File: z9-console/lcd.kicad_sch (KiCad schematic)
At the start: 17 parts, among them J10 Conn_01x04_Pin, J2 LCD 3.2" 240x320 Conn_01x14_P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, J8 Conn_01x14_Pin, J9 Conn_01x18_Pin, Q2 AO3400A, Q4 NPN, U7 SN74LVC1G14DRLR, U8 XC6206PxxxMR

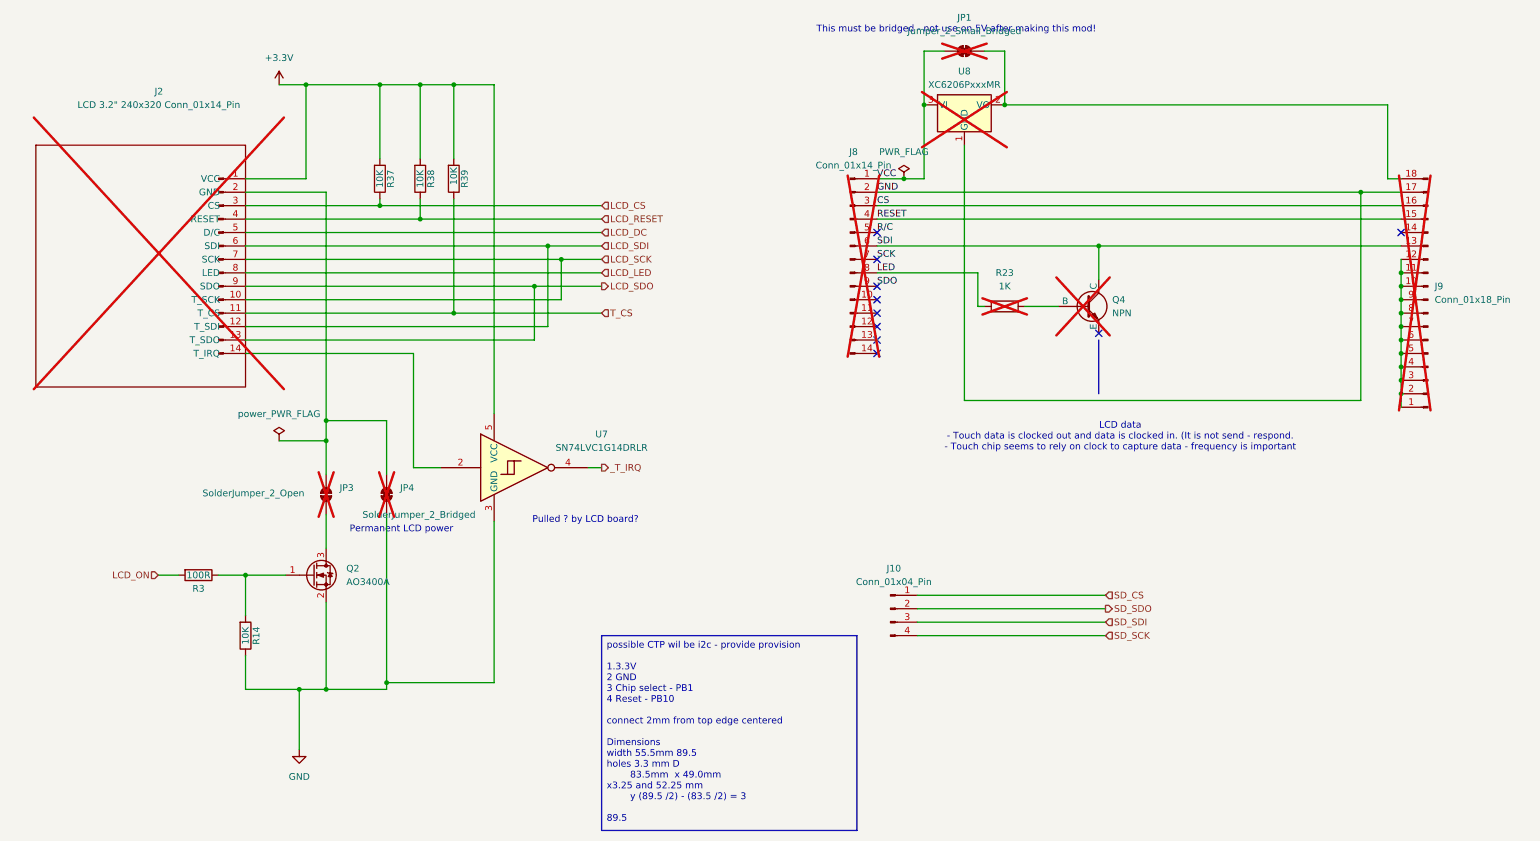
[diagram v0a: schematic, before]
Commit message: lcd power switch-- add new accelerometer
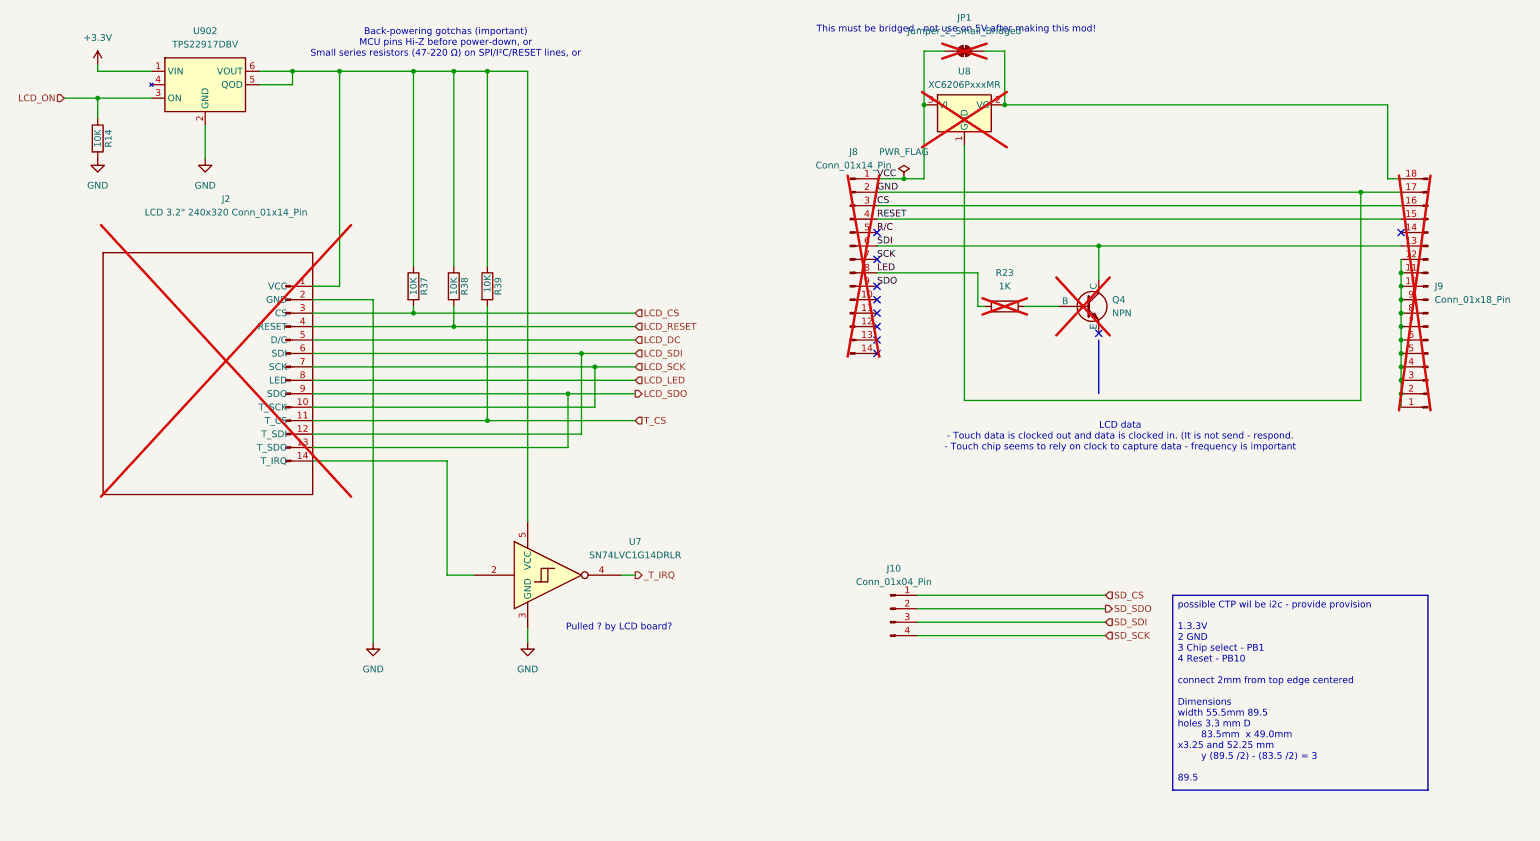
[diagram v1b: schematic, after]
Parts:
- removed JP3: SolderJumper_2_Open, Jumper:SolderJumper-2_P1.3mm_Open_TrianglePad1.0x1.5mm, symbol Jumper:SolderJumper_2_Open
- removed JP4: SolderJumper_2_Bridged, Jumper:SolderJumper-2_P1.3mm_Bridged_Pad1.0x1.5mm, symbol Jumper:SolderJumper_2_Bridged
- removed Q2: AO3400A, Package_TO_SOT_SMD:SOT-23, symbol dnt_global:AO3400A
- removed R3: 100R, Resistor_SMD:R_0603_1608Metric, symbol Device:R
- added U902: TPS22917DBV, dnt:SOT-363_SC-70-6, symbol dnt_global:TPS22919DCKR
- R14, R37, R38, R39: footprint Resistor_SMD:R_0603_1608Metric -> PCM_JLCPCB:R_0402; symbol Device:R -> dnt_global:Resistor_0402,10kΩ; Attrition Qty (none) -> 10; Category (none) -> Resistors,Chip Resistor - Surface Mount; Class (none) -> Basic Component; LCSC C25804 -> C25744; Manufacturer (none) -> UNI-ROYAL(Uniroyal Elec); Minimum Qty (none) -> 20; Operating Temperature Range (none) -> -55°C~+155°C; Overload Voltage (Max) (none) -> 50V; Part (none) -> 0402WGF1002TCE; Power(Watts) (none) -> 62.5mW; Price (none) -> 0.004USD; Process (none) -> SMT; Resistance (none) -> 10kΩ; Stock (none) -> 24372091; Temperature Coefficient (none) -> ±100ppm/°C; Tolerance (none) -> ±1%; Type (none) -> Thick Film Resistors
- R23: footprint Resistor_SMD:R_0201_0603Metric -> PCM_JLCPCB:R_0402; symbol Device:R -> dnt_global:Resistor_0402,10kΩ; Attrition Qty (none) -> 10; Category (none) -> Resistors,Chip Resistor - Surface Mount; Class (none) -> Basic Component; LCSC (none) -> C25744; Manufacturer (none) -> UNI-ROYAL(Uniroyal Elec); Minimum Qty (none) -> 20; Operating Temperature Range (none) -> -55°C~+155°C; Overload Voltage (Max) (none) -> 50V; Part (none) -> 0402WGF1002TCE; Power(Watts) (none) -> 62.5mW; Price (none) -> 0.004USD; Process (none) -> SMT; Resistance (none) -> 10kΩ; Stock (none) -> 24372091; Temperature Coefficient (none) -> ±100ppm/°C; Tolerance (none) -> ±1%; Type (none) -> Thick Film Resistors
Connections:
- net +3.3V: now also U902.1 (VIN); no longer J2.1 (VCC), R37.2, R38.2, R39.2, U7.5 (VCC)
- net GND: now also J2.2 (GND), U902.2 (GND)
- net LCD_ON: now also R14.2, U902.3 (ON)
- new net: J2.1 (VCC), R37.2, R38.2, R39.2, U7.5 (VCC), U902.5 (QOD), U902.6 (VOUT)
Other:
- note added: "Back-powering gotchas (important) MCU pins Hi-Z before power-down, or Small series resistors (47-220 Ω) on SPI/I²C/RESET lines, or"
- note removed: "Permanent LCD power"
- moved on the sheet: J2, R14, R37, R38, R39, U7

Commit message: change MEMS device
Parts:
- renumbered J8 to J3, J10 to J4, J9 to J5, JP1 to JP2, Q4 to Q2, R14 to R2, R37 to R3, R38 to R4, R39 to R5, R23 to R6, U902 to U2, U7 to U3, U8 to U4
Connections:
- net +3.3V: now also U3.5 (VCC)
- net at J2.1 (VCC), R3.2, R4.2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: no longer U3.5 (VCC)
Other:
- note added: "Pulled low by LCD board on touch - needs invertor"
- note removed: "Pulled ? by LCD board?"
- moved on the sheet: J4

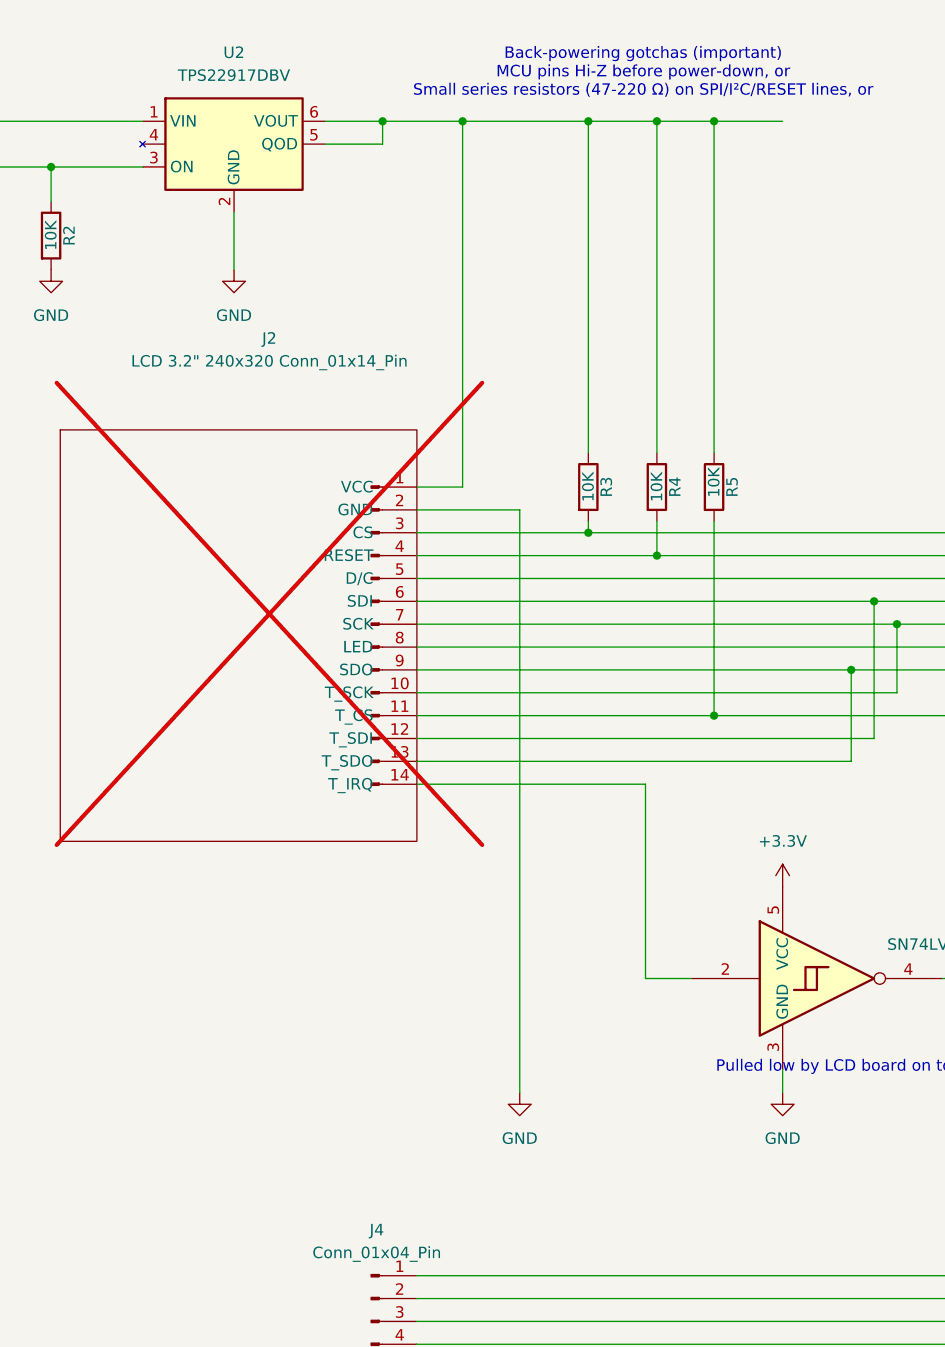
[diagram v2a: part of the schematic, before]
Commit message: drc con - fix ti switch reference  - fix stm32  bypass
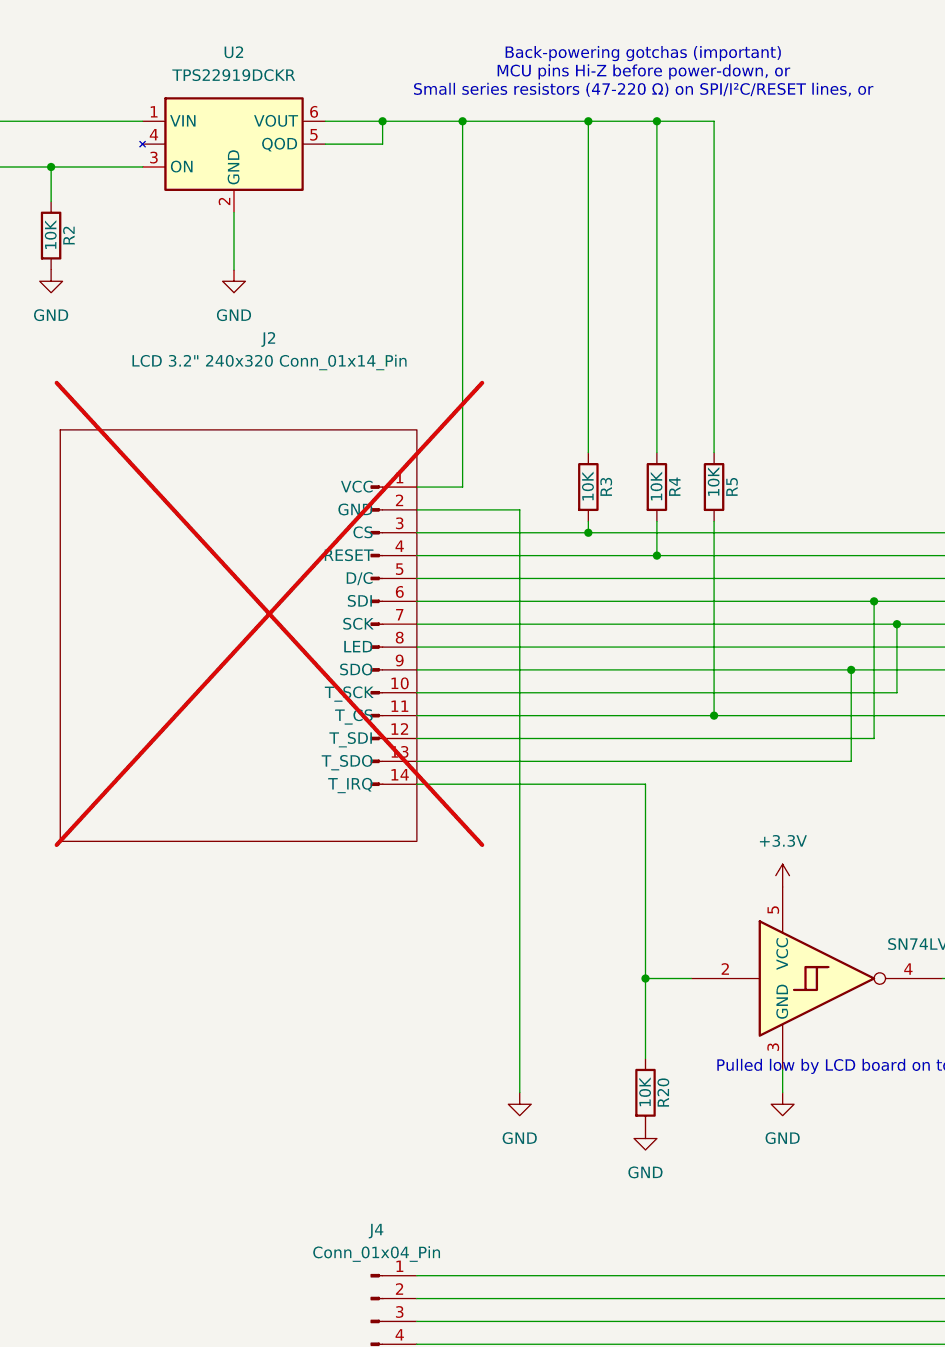
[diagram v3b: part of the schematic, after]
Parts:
- added R20: 10K, PCM_JLCPCB:R_0402, symbol dnt_global:Resistor_0402,10kΩ
- U2: value TPS22917DBV -> TPS22919DCKR
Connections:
- net GND: now also R20.1
- net at J2.14 (T_IRQ), U3.2: now also R20.2

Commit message: lcsc components and cleanup
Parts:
- U2: LCSC (none) -> C2149796
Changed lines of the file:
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@@
+			)
+		)
+		(property "LCSC" "C2149796"
+			(at 51.308 15.748 0)
+			(effects
+				(font
+					(size 1.27 1.27)
+				)
+				(hide yes)
 			)
 		)

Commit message: lcsc changes done - export for prod
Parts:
- R2, R20, R3, R4, R5: footprint PCM_JLCPCB:R_0402 -> dnt:R_0402_1005Metric; symbol dnt_global:Resistor_0402,10kΩ -> dnt_global:0402,10kΩ
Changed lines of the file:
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@@
 	)
 	(symbol
-		(lib_id "dnt_global:Resistor_0402,10kΩ")
+		(lib_id "dnt_global:0402,10kΩ")
 		(at 104.14 63.5 0)
 		(mirror x)
@@
 			)
 		)
-		(property "Footprint" "PCM_JLCPCB:R_0402"
+		(property "Footprint" "dnt:R_0402_1005Metric"
 			(at 102.362 63.5 90)
 			(effects
@@
 	)
 	(symbol
-		(lib_id "dnt_global:Resistor_0402,10kΩ")
+		(lib_id "dnt_global:0402,10kΩ")
 		(at 96.52 130.81 0)
 		(mirror x)
@@
 			)
 		)
-		(property "Footprint" "PCM_JLCPCB:R_0402"
+		(property "Footprint" "dnt:R_0402_1005Metric"
 			(at 94.742 130.81 90)
 			(effects
@@
 	)
 	(symbol
-		(lib_id "dnt_global:Resistor_0402,10kΩ")
+		(lib_id "dnt_global:0402,10kΩ")
 		(at 97.79 63.5 0)
 		(mirror x)
@@
 			)
 		)
-		(property "Footprint" "PCM_JLCPCB:R_0402"
+		(property "Footprint" "dnt:R_0402_1005Metric"
 			(at 96.012 63.5 90)
 			(effects
@@
 	)
 	(symbol
-		(lib_id "dnt_global:Resistor_0402,10kΩ")
+		(lib_id "dnt_global:0402,10kΩ")
 		(at 30.48 35.56 0)
 		(mirror x)
@@
 			)
 		)
-		(property "Footprint" "PCM_JLCPCB:R_0402"
+		(property "Footprint" "dnt:R_0402_1005Metric"
 			(at 28.702 35.56 90)
 			(effects
@@
 	)
 	(symbol
-		(lib_id "dnt_global:Resistor_0402,10kΩ")
+		(lib_id "dnt_global:0402,10kΩ")
 		(at 90.17 63.5 0)
 		(mirror x)
@@
 			)
 		)
-		(property "Footprint" "PCM_JLCPCB:R_0402"
+		(property "Footprint" "dnt:R_0402_1005Metric"
 			(at 88.392 63.5 90)
 			(effects

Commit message: sheet updates
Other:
- company: (none) -> Zero9 -  0-9.au
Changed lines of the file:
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@@
 	(generator_version "9.0")
 	(paper "A4")
+	(title_block
+		(company "Zero9 -  0-9.au")
+		(comment 1 "Some schematic is shared ")
+	)
 	(text "Back-powering gotchas (important)\nMCU pins Hi-Z before power-down, or\nSmall series resistors (47-220 Ω) on SPI/I²C/RESET lines, or\n"
 		(exclude_from_sim no)
